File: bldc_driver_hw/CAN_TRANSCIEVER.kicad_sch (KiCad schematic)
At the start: 16 parts, among them U8 SN65HVD234

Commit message: schematic finished pcb in progress
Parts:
- added TP36, TP37: TestPoint, TestPoint:TestPoint_Pad_D2.0mm, symbol Connector:TestPoint
- renumbered C67 to C72, C68 to C73, C72 to C74, C69 to C75, C70 to C76, C71 to C77, D21 to D19, L2 to L3, R74 to R75, R75 to R76, R73 to R77, R72 to R78, R70 to R79, R71 to R80, R76 to R81, U8 to U12
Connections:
- net CAN_RX: now also TP36.1
- net CAN_TX: now also TP37.1
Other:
- moved on the sheet: C74

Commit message: Board finished to review
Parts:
- removed TP36, TP37: TestPoint, TestPoint:TestPoint_Pad_D2.0mm, symbol Connector:TestPoint

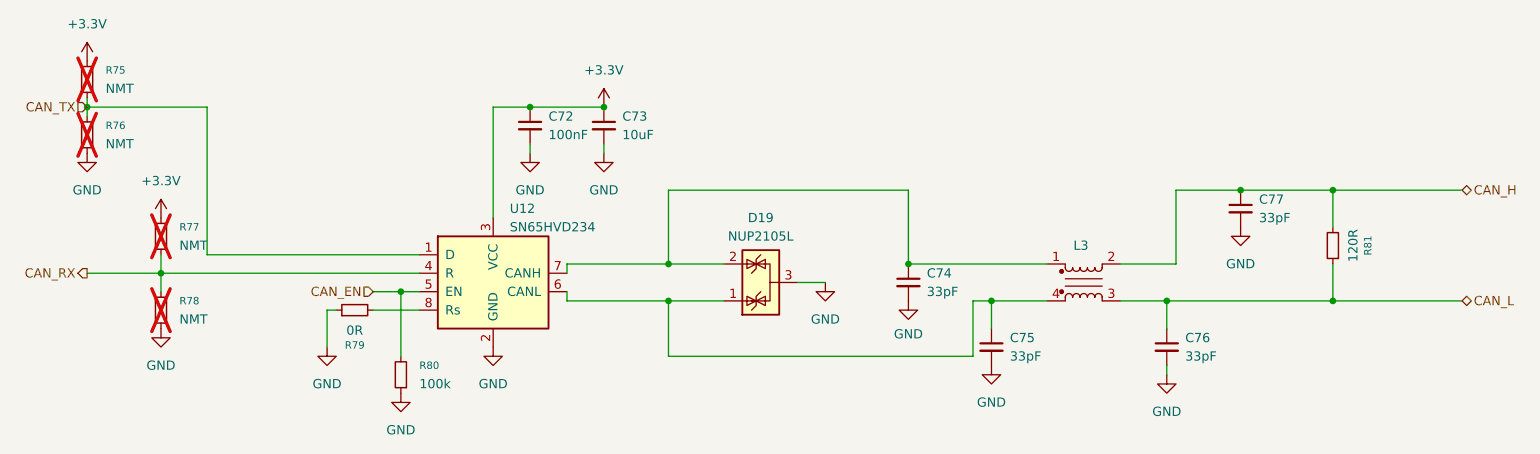
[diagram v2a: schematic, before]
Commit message: added lcsc codes
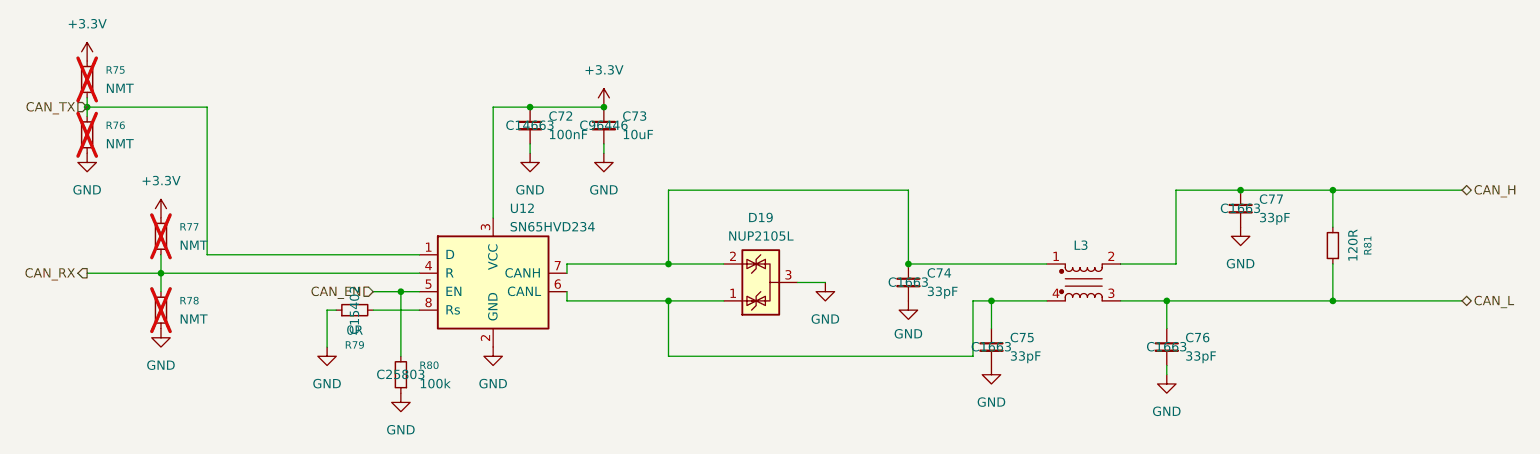
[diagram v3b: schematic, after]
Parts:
- C72: LCSC (none) -> C14663
- C73: LCSC (none) -> C96446
- C74, C75, C76, C77: LCSC (none) -> C1663
- R79: LCSC (none) -> C15402
- R80: LCSC (none) -> C25803

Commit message: finished_board
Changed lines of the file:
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@@
 					(size 1.27 1.27)
 				)
+				(hide yes)
 			)
 		)
@@
 					(size 1.27 1.27)
 				)
+				(hide yes)
 			)
 		)
@@
 					(size 1.27 1.27)
 				)
+				(hide yes)
 			)
 		)
@@
 					(size 1.27 1.27)
 				)
+				(hide yes)
 			)
 		)
@@
 					(size 1.27 1.27)
 				)
+				(hide yes)
 			)
 		)
@@
 					(size 1.27 1.27)
 				)
+				(hide yes)
 			)
 		)
@@
 					(size 1.27 1.27)
 				)
+				(hide yes)
 			)
 		)
@@
 					(size 1.27 1.27)
 				)
-			)
-		)
+				(hide yes)
+			)
+		)

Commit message: finished
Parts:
- D19, L3, R81, U12: now left out of the parts list
- R75, R76, R77, R78: now fitted; now left out of the parts list
- R79: LCSC C15402 -> C21189
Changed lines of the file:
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@@
 		(unit 1)
 		(exclude_from_sim no)
-		(in_bom yes)
+		(in_bom no)
 		(on_board yes)
 		(dnp no)
@@
 		(unit 1)
 		(exclude_from_sim no)
-		(in_bom yes)
-		(on_board yes)
-		(dnp yes)
+		(in_bom no)
+		(on_board yes)
+		(dnp no)
 		(fields_autoplaced yes)
 		(property "Reference" "R78"
@@
 		(unit 1)
 		(exclude_from_sim no)
-		(in_bom yes)
+		(in_bom no)
 		(on_board yes)
 		(dnp no)
@@
 		(unit 1)
 		(exclude_from_sim no)
-		(in_bom yes)
+		(in_bom no)
 		(on_board yes)
 		(dnp no)
@@
 			)
 		)
-		(property "LCSC" "C15402"
+		(property "LCSC" "C21189"
 			(at 78.74 118.11 0)
 			(effects
@@
 		(unit 1)
 		(exclude_from_sim no)
-		(in_bom yes)
-		(on_board yes)
-		(dnp yes)
+		(in_bom no)
+		(on_board yes)
+		(dnp no)
 		(fields_autoplaced yes)
 		(property "Reference" "R76"
@@
 		(unit 1)
 		(exclude_from_sim no)
-		(in_bom yes)
-		(on_board yes)
-		(dnp yes)
+		(in_bom no)
+		(on_board yes)
+		(dnp no)
 		(property "Reference" "R77"
 			(at 54.61 106.6799 0)
@@
 		(unit 1)
 		(exclude_from_sim no)
-		(in_bom yes)
+		(in_bom no)
 		(on_board yes)
 		(dnp no)
@@
 		(unit 1)
 		(exclude_from_sim no)
-		(in_bom yes)
-		(on_board yes)
-		(dnp yes)
+		(in_bom no)
+		(on_board yes)
+		(dnp no)
 		(fields_autoplaced yes)
 		(property "Reference" "R75"
